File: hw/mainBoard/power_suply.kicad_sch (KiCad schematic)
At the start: 3 parts, among them U2 AMS1117-3.3

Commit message: hw
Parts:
- removed C4, C5: 22uF, symbol Device:C
- removed U2: AMS1117-3.3, Package_TO_SOT_SMD:SOT-223-3_TabPin2, symbol Regulator_Linear:AMS1117-3.3
- added C11: 2.2uF, symbol Device:C
- added C12, C14: 100nF, symbol Device:C
- added C13: 4.7uF, symbol Device:C
- added C15: 10uF, symbol Device:C
- added L1: 2.7uH, symbol Device:L
- added Q1, Q2: NMOS, symbol Simulation_SPICE:NMOS
- added R10: 25m, symbol Device:R
- added R4, R5: 100k, symbol Device:R
- added R6: 40.2k, symbol Device:R
- added R7: 9.53k, symbol Device:R
- added R8: 59k, symbol Device:R
- added R9: 10k, symbol Device:R
- added U2: LM5148RGYR, VQFN24_RGY_TEX, symbol LM5148:LM5148RGYR
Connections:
- net GND: now also C11.2, C12.2, C13.2, C15.2, Q2.3 (S), R6.1, R7.1, R9.1, U2.10 (PGND), U2.16 (VCCX), U2.25 (EPAD), U2.7 (AGND)
- new net: R6.2, U2.3 (CNFG)
- new net: C14.1, L1.2, Q1.3 (S), Q2.1 (D), U2.14 (SW)
- new net: C14.2, U2.15 (CBOOT)
- new net: C12.1, R5.2, U2.18 (PFM/SYNC), U2.8 (VDDA)
- new net: C11.1, R4.2, U2.9 (VCC)
- new net: R8.1, R9.2, U2.6 (FB)
- new net: L1.1, R10.2, U2.20 (ISNS+)
- new net: Q1.2 (G), U2.13 (HO)
- new net: Q2.2 (G), U2.11 (LO)
- new net: R4.1, U2.17 (PG/SYNCOUT)
- new net: R7.2, U2.4 (RT)
- new net: R5.1, U2.5 (EXTCOMP)
- new net 5.5V: C15.1, R10.1, R8.2, U2.21 (VOUT)
- new net EXT_24V: C13.1, Q1.1 (D), U2.12 (VIN)
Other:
- note added: "Output from buck"
- note added: "TODO: change to 5.2V"
- note removed: "Need to be changed to at least 12 V and to use different parts..."

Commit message: hw + blok schema
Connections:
- net EXT_24V renamed 24V
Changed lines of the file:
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@@
     (effects (font (size 1.27 1.27)) (justify left bottom))
   )
-  (global_label "5.5V" (shape input) (at 121.92 31.75 180) (fields_autoplaced)
+  (hierarchical_label "24V" (shape input) (at 160.02 68.58 180) (fields_autoplaced)
     (effects (font (size 1.27 1.27)) (justify right))
-    (property "Intersheetrefs" "${INTERSHEET_REFS}" (at 114.8224 31.75 0)
-      (effects (font (size 1.27 1.27)) (justify right) hide)
-    )
   )
-  (global_label "EXT_24V" (shape input) (at 160.02 68.58 180) (fields_autoplaced)
+  (hierarchical_label "5.5V" (shape output) (at 121.92 31.75 180) (fields_autoplaced)
     (effects (font (size 1.27 1.27)) (justify right))
-    (property "Intersheetrefs" "${INTERSHEET_REFS}" (at 149.2335 68.58 0)
-      (effects (font (size 1.27 1.27)) (justify right) hide)
-    )
   )
   (symbol (lib_id "Device:R") (at 34.29 85.09 180) (unit 1)

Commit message: schematka
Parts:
- removed C11: 2.2uF, symbol Device:C
- removed C12, C14: 100nF, symbol Device:C
- removed C13: 4.7uF, symbol Device:C
- removed C15: 10uF, symbol Device:C
- removed L1: 2.7uH, symbol Device:L
- removed Q1, Q2: NMOS, symbol Simulation_SPICE:NMOS
- removed R10: 25m, symbol Device:R
- removed R4, R5: 100k, symbol Device:R
- removed R6: 40.2k, symbol Device:R
- removed R7: 9.53k, symbol Device:R
- removed R8: 59k, symbol Device:R
- removed R9: 10k, symbol Device:R
- removed U2: LM5148RGYR, VQFN24_RGY_TEX, symbol LM5148:LM5148RGYR
- added C10, C17: 100nF, symbol Device:C
- added C16: 2.2uF, symbol Device:C
- added C8: 10uF, symbol Device:C
- added C9: 4.7uF, symbol Device:C
- added L2: 2.7uH, symbol Device:L
- added Q3, Q4: NMOS, symbol Simulation_SPICE:NMOS
- added R14: 40.2k, symbol Device:R
- added R15: 10k, symbol Device:R
- added R16: 54.9k, symbol Device:R
- added R17: 9.53k, symbol Device:R
- added R18, R19: 100k, symbol Device:R
- added R20: 25m, symbol Device:R
- added U6: LM5148RGYR, VQFN24_RGY_TEX, symbol LM5148:LM5148RGYR
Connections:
- net 24V: now also C9.1, Q3.1 (D), U6.12 (VIN), U6.19 (EN)
- net GND: now also C10.2, C16.2, C8.2, C9.2, Q4.3 (S), R14.1, R15.2, R17.2, U6.10 (PGND), U6.16 (VCCX), U6.25 (EPAD), U6.7 (AGND)
- new net: C16.1, R19.1, U6.9 (VCC)
- new net: R17.1, U6.4 (RT)
- new net: C17.2, L2.2, Q3.3 (S), Q4.1 (D), U6.14 (SW)
- new net: C17.1, U6.15 (CBOOT)
- new net: R18.2, U6.5 (EXTCOMP)
- new net: Q4.2 (G), U6.11 (LO)
- new net: Q3.2 (G), U6.13 (HO)
- new net: R19.2, U6.17 (PG/SYNCOUT)
- new net: R14.2, U6.3 (CNFG)
- new net: R15.1, R16.2, U6.6 (FB)
- new net 5.2V: C8.1, R16.1, R20.1, U6.21 (VOUT)
- new net ISNS+: L2.1, R20.2, U6.20 (ISNS+)
- new net VDDA: C10.1, R18.1, U6.18 (PFM/SYNC), U6.8 (VDDA)
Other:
- note added: "From external power suply"
- note removed: "TODO: change to 5.2V"

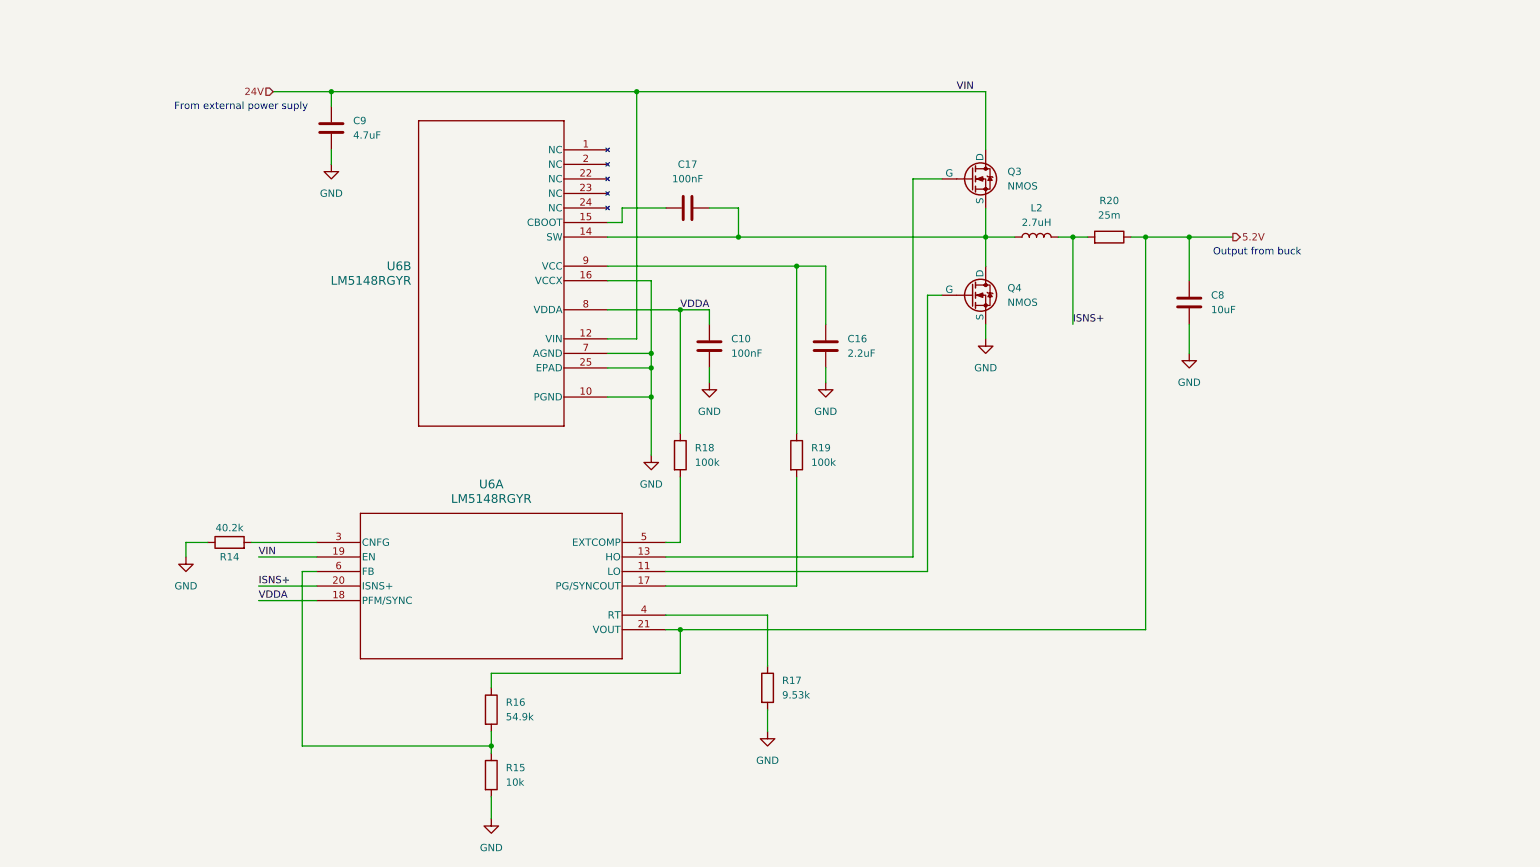
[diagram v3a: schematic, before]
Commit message: text - napajeci obvod, ochrany, 230v + pomocne schema v kicadu
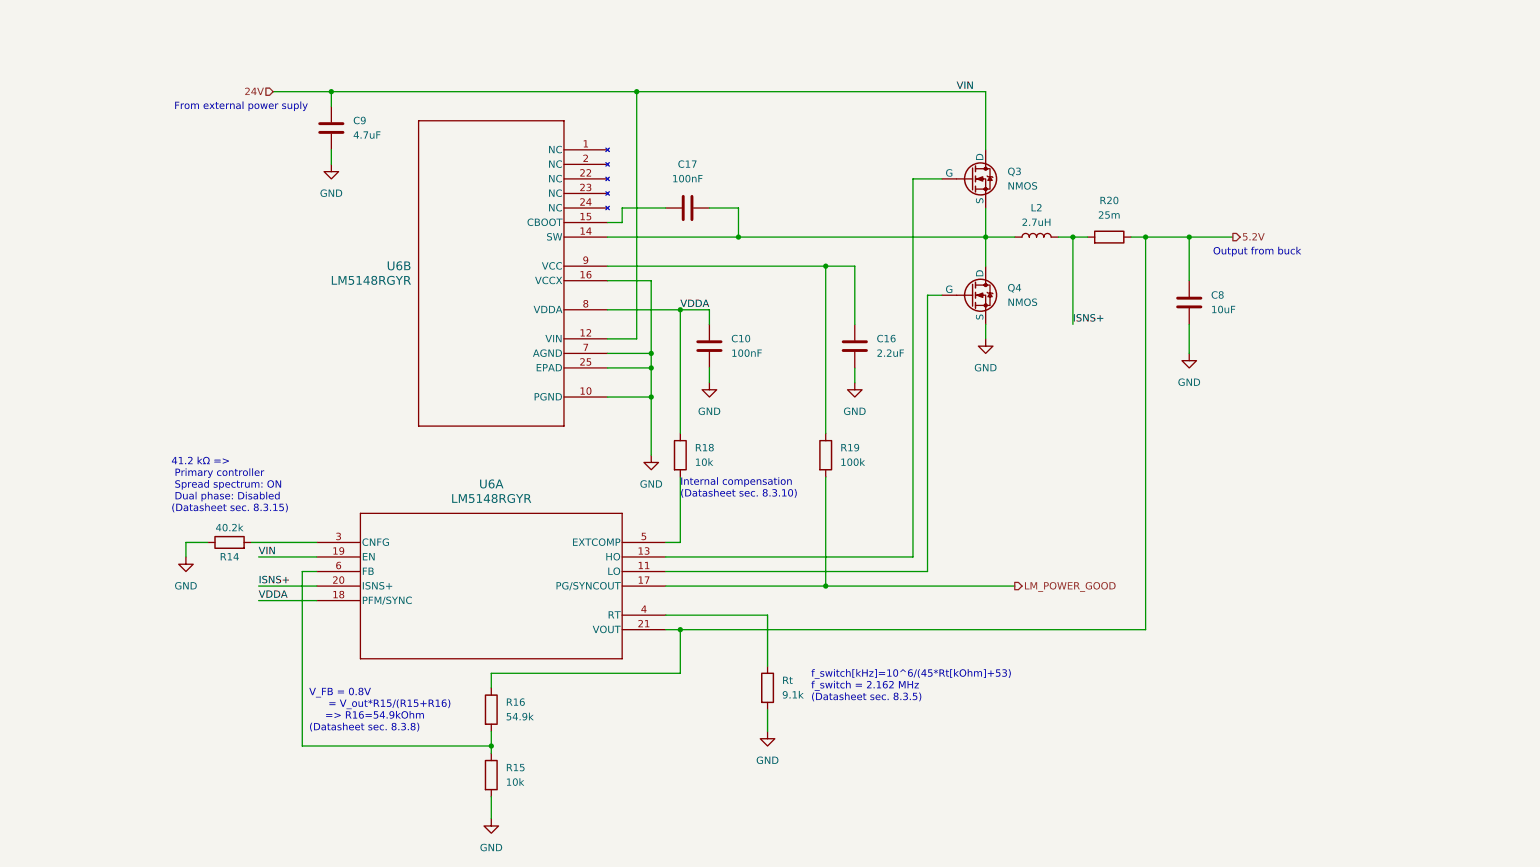
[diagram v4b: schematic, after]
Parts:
- R18: value 100k -> 10k
- Rt: renamed from R17; value 9.53k -> 9.1k
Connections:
- net LM_POWER_GOOD: now reaches R19.2, U6.17 (PG/SYNCOUT)
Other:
- note added: "41.2 kΩ => Primary controller Spread spectrum: ON Dual phase: Disabled (Datasheet sec. 8.3.15)"
- note added: "Internal compensation (Datasheet sec. 8.3.10)"
- note added: "V_FB = 0.8V = V_out*R15/(R15+R16) => R16=54.9kOhm (Datasheet sec. 8.3.8)"
- note added: "f_switch[kHz]=10^6/(45*Rt[kOhm]+53) f_switch = 2.162 MHz (Datasheet sec. 8.3.5)"
- moved on the sheet: C16, R19
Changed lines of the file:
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@@
   (junction (at 76.2 30.48) (diameter 0) (color 0 0 0 0)
   )
+  (junction (at 162.56 60.96) (diameter 0) (color 0 0 0 0)
+  )
   (junction (at 104.14 144.78) (diameter 0) (color 0 0 0 0)
   )
   (junction (at 147.32 55.88) (diameter 0) (color 0 0 0 0)
   )
+  (junction (at 162.56 116.84) (diameter 0) (color 0 0 0 0)
+  )
   (junction (at 132.08 78.74) (diameter 0) (color 0 0 0 0)
   )
@@
   (junction (at 137.16 124.46) (diameter 0) (color 0 0 0 0)
   )
-  (junction (at 157.48 60.96) (diameter 0) (color 0 0 0 0)
-  )
   (junction (at 132.08 83.82) (diameter 0) (color 0 0 0 0)
   )
@@
     (stroke (width 0) (type default))
   )
-  (wire (pts (xy 162.56 78.74) (xy 162.56 81.28))
+  (wire (pts (xy 167.64 78.74) (xy 167.64 81.28))
     (stroke (width 0) (type default))
   )
@@
     (stroke (width 0) (type default))
   )
+  (wire (pts (xy 162.56 60.96) (xy 167.64 60.96))
+    (stroke (width 0) (type default))
+  )
   (wire (pts (xy 129.54 30.48) (xy 129.54 73.66))
     (stroke (width 0) (type default))
@@
     (stroke (width 0) (type default))
   )
-  (wire (pts (xy 157.48 60.96) (xy 162.56 60.96))
-    (stroke (width 0) (type default))
-  )
   (wire (pts (xy 134.62 124.46) (xy 137.16 124.46))
     (stroke (width 0) (type default))
@@
     (stroke (width 0) (type default))
   )
-  (wire (pts (xy 157.48 60.96) (xy 124.46 60.96))
+  (wire (pts (xy 162.56 116.84) (xy 195.58 116.84))
     (stroke (width 0) (type default))
   )
@@
     (stroke (width 0) (type default))
   )
+  (wire (pts (xy 124.46 60.96) (xy 162.56 60.96))
+    (stroke (width 0) (type default))
+  )
   (wire (pts (xy 205.74 71.12) (xy 205.74 55.88))
     (stroke (width 0) (type default))
@@
     (stroke (width 0) (type default))
   )
-  (wire (pts (xy 157.48 97.79) (xy 157.48 116.84))
+  (wire (pts (xy 162.56 97.79) (xy 162.56 116.84))
     (stroke (width 0) (type default))
   )
@@
     (stroke (width 0) (type default))
   )
-  (wire (pts (xy 134.62 116.84) (xy 157.48 116.84))
+  (wire (pts (xy 134.62 116.84) (xy 162.56 116.84))
     (stroke (width 0) (type default))
   )
@@
     (stroke (width 0) (type default))
   )
-  (wire (pts (xy 157.48 90.17) (xy 157.48 60.96))
+  (wire (pts (xy 162.56 90.17) (xy 162.56 60.96))
     (stroke (width 0) (type default))
   )
@@
     (stroke (width 0) (type default))
   )
-  (wire (pts (xy 162.56 71.12) (xy 162.56 60.96))
+  (wire (pts (xy 167.64 71.12) (xy 167.64 60.96))
     (stroke (width 0) (type default))
   )
@@
   )
   (text "From external power suply" (at 48.7471 33.9083 0)
+    (effects (font (size 1.27 1.27)) (justify left bottom))
+  )
+  (text "f_switch[kHz]=10^6/(45*Rt[kOhm]+53)\nf_switch = 2.162 MHz\n(Datasheet sec. 8.3.5)"
+    (at 160.02 137.16 0)
     (effects (font (size 1.27 1.27)) (justify left bottom))
   )
@@
     (effects (font (size 1.27 1.27)) (justify right bottom))
   )
+  (text "41.2 kΩ =>\n Primary controller\n Spread spectrum: ON\n Dual phase: Disabled\n(Datasheet sec. 8.3.15)"
+    (at 48.26 104.14 0)
+    (effects (font (size 1.27 1.27)) (justify left bottom))
+  )
+  (text "Internal compensation\n(Datasheet sec. 8.3.10)" (at 137.16 101.6 0)
+    (effects (font (size 1.27 1.27)) (justify left bottom))
+  )
+  (text "V_FB = 0.8V \n      = V_out*R15/(R15+R16)\n	 => R16=54.9kOhm\n(Datasheet sec. 8.3.8)"
+    (at 72.3291 142.4326 0)
+    (effects (font (size 1.27 1.27)) (justify left bottom))
+  )
   (label "ISNS+" (at 205.74 71.12 0) (fields_autoplaced)
     (effects (font (size 1.27 1.27)) (justify left bottom))
@@
   (label "VDDA" (at 63.5 119.38 0) (fields_autoplaced)
     (effects (font (size 1.27 1.27)) (justify left bottom))
+  )
+  (hierarchical_label "LM_POWER_GOOD" (shape output) (at 195.58 116.84 0) (fields_autoplaced)
+    (effects (font (size 1.27 1.27)) (justify left))
   )
   (hierarchical_label "24V" (shape input) (at 66.04 30.48 180) (fields_autoplaced)
@@
     )
   )
-  (symbol (lib_id "Device:C") (at 162.56 74.93 0) (unit 1)
-    (in_bom yes) (on_board yes) (dnp no) (fields_autoplaced)
-    (property "Reference" "C16" (at 166.37 73.66 0)
-      (effects (font (size 1.27 1.27)) (justify left))
-    )
-    (property "Value" "2.2uF" (at 166.37 76.2 0)
-      (effects (font (size 1.27 1.27)) (justify left))
-    )
-    (property "Footprint" "" (at 163.5252 78.74 0)
-      (effects (font (size 1.27 1.27)) hide)
-    )
-    (property "Datasheet" "~" (at 162.56 74.93 0)
+  (symbol (lib_id "Device:C") (at 167.64 74.93 0) (unit 1)
+    (in_bom yes) (on_board yes) (dnp no) (fields_autoplaced)
+    (property "Reference" "C16" (at 171.45 73.66 0)
+      (effects (font (size 1.27 1.27)) (justify left))
+    )
+    (property "Value" "2.2uF" (at 171.45 76.2 0)
+      (effects (font (size 1.27 1.27)) (justify left))
+    )
+    (property "Footprint" "" (at 168.6052 78.74 0)
+      (effects (font (size 1.27 1.27)) hide)
+    )
+    (property "Datasheet" "~" (at 167.64 74.93 0)
       (effects (font (size 1.27 1.27)) hide)
     )
@@
   (symbol (lib_id "Device:R") (at 152.4 134.62 0) (unit 1)
     (in_bom yes) (on_board yes) (dnp no) (fields_autoplaced)
-    (property "Reference" "R17" (at 154.94 133.35 0)
-      (effects (font (size 1.27 1.27)) (justify left))
-    )
-    (property "Value" "9.53k" (at 154.94 135.89 0)
+    (property "Reference" "Rt" (at 154.94 133.35 0)
+      (effects (font (size 1.27 1.27)) (justify left))
+    )
+    (property "Value" "9.1k" (at 154.94 135.89 0)
       (effects (font (size 1.27 1.27)) (justify left))
     )
@@
       (project "mainBoard"
         (path "/afbe4b5f-4e5c-4a12-a44b-208d158a3f7a/d2d24d60-9ae9-4639-8ba0-76ed40df3c00"
-          (reference "R17") (unit 1)
+          (reference "Rt") (unit 1)
         )
       )
@@
       (effects (font (size 1.27 1.27)) (justify left))
     )
-    (property "Value" "100k" (at 139.7 95.25 0)
+    (property "Value" "10k" (at 139.7 95.25 0)
       (effects (font (size 1.27 1.27)) (justify left))
     )
@@
     )
   )
-  (symbol (lib_id "Device:R") (at 157.48 93.98 0) (unit 1)
-    (in_bom yes) (on_board yes) (dnp no) (fields_autoplaced)
-    (property "Reference" "R19" (at 160.02 92.71 0)
-      (effects (font (size 1.27 1.27)) (justify left))
-    )
-    (property "Value" "100k" (at 160.02 95.25 0)
-      (effects (font (size 1.27 1.27)) (justify left))
-    )
-    (property "Footprint" "" (at 155.702 93.98 90)
-      (effects (font (size 1.27 1.27)) hide)
-    )
-    (property "Datasheet" "~" (at 157.48 93.98 0)
+  (symbol (lib_id "Device:R") (at 162.56 93.98 0) (unit 1)
+    (in_bom yes) (on_board yes) (dnp no) (fields_autoplaced)
+    (property "Reference" "R19" (at 165.1 92.71 0)
+      (effects (font (size 1.27 1.27)) (justify left))
+    )
+    (property "Value" "100k" (at 165.1 95.25 0)
+      (effects (font (size 1.27 1.27)) (justify left))
+    )
+    (property "Footprint" "" (at 160.782 93.98 90)
+      (effects (font (size 1.27 1.27)) hide)
+    )
+    (property "Datasheet" "~" (at 162.56 93.98 0)
       (effects (font (size 1.27 1.27)) hide)
     )
@@
     )
   )
-  (symbol (lib_id "power:GND") (at 162.56 81.28 0) (mirror y) (unit 1)
-    (in_bom yes) (on_board yes) (dnp no) (fields_autoplaced)
-    (property "Reference" "#PWR037" (at 162.56 87.63 0)
-      (effects (font (size 1.27 1.27)) hide)
-    )
-    (property "Value" "GND" (at 162.56 86.36 0)
-      (effects (font (size 1.27 1.27)))
-    )
-    (property "Footprint" "" (at 162.56 81.28 0)
-      (effects (font (size 1.27 1.27)) hide)
-    )
-    (property "Datasheet" "" (at 162.56 81.28 0)
-      (effects (font (size 1.27 1.27)) hide)
-    )
+  (symbol (lib_id "power:GND") (at 167.64 81.28 0) (mirror y) (unit 1)
+    (in_bom yes) (on_board yes) (dnp no) (fields_autoplaced)
+    (property "Reference" "#PWR037" (at 167.64 87.63 0)
+      (effects (font (size 1.27 1.27)) hide)
+    )
+    (property "Value" "GND" (at 167.64 86.36 0)
+      (effects (font (size 1.27 1.27)))
+    )
+    (property "Footprint" "" (at 167.64 81.28 0)
+      (effects (font (size 1.27 1.27)) hide)
+    )
+    (property "Datasheet" "" (at 167.64 81.28 0)
+      (effects (font (size 1.27 1.27)) hide)
+    )

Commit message: drawing layout
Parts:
- C10, C16, C17, C8, C9: footprint (none) -> Capacitor_SMD:C_1206_3216Metric_Pad1.33x1.80mm_HandSolder
- L2: footprint (none) -> Inductor_SMD:L_Bourns-SRN8040_8x8.15mm
- Q3: footprint (none) -> DQJ8; symbol Simulation_SPICE:NMOS -> NMOS-CSD18534:CSD18534Q5A
- Q4: footprint (none) -> DQJ0008A; symbol Simulation_SPICE:NMOS -> NMOS-CSD18514:CSD18514Q5A
- R14, R15, R16, R18, R19, R20: footprint (none) -> Resistor_SMD:R_0805_2012Metric_Pad1.20x1.40mm_HandSolder
- Rt1: renamed from Rt; footprint (none) -> Resistor_SMD:R_0805_2012Metric_Pad1.20x1.40mm_HandSolder
- U6: footprint VQFN24_RGY_TEX -> LM5148:VQFN24_RGY_TEX
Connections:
- net 24V: now also Q3.5, Q3.6 (D), Q3.7 (D), Q3.8 (D), Q3.9; no longer Q3.1 (D)
- net GND: now also Q4.1, Q4.2 (S); no longer Q4.3 (S)
- net at C17.2, L2.2, U6.14 (SW): now also Q3.1, Q3.2 (S), Q4.5, Q4.6 (D), Q4.7 (D), Q4.8 (D), Q4.9; no longer Q3.3 (S), Q4.1 (D)
- net at U6.11 (LO): now also Q4.4; no longer Q4.2 (G)
- net at U6.13 (HO): now also Q3.4; no longer Q3.2 (G)
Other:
- moved on the sheet: C9, R14

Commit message: buck vedle
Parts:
- removed Q3: NMOS, DQJ8, symbol NMOS-CSD18534:CSD18534Q5A
- added C15, C18, C19: 47uF, Capacitor_SMD:C_1210_3225Metric_Pad1.33x2.70mm_HandSolder, symbol Device:C
- added C20, C21: 10uF, Capacitor_SMD:C_1210_3225Metric_Pad1.33x2.70mm_HandSolder, symbol Device:C
- added C22: 470nF, Capacitor_SMD:C_0805_2012Metric_Pad1.18x1.45mm_HandSolder, symbol Device:C
- added C23, C24, C25, C26: 0.01uF, Capacitor_SMD:C_0805_2012Metric_Pad1.18x1.45mm_HandSolder, symbol Device:C
- added C27: 22p, Capacitor_SMD:C_0805_2012Metric_Pad1.18x1.45mm_HandSolder, symbol Device:C
- added NT1: NetTie_2, NetTie:NetTie-2_SMD_Pad0.5mm, symbol Device:NetTie_2
- added Q1: NMOS, DQJ0008A, symbol NMOS-CSD18514:CSD18514Q5A
- added R3: 10k, Resistor_SMD:R_0805_2012Metric_Pad1.20x1.40mm_HandSolder, symbol Device:R
- C10, C17: footprint Capacitor_SMD:C_1206_3216Metric_Pad1.33x1.80mm_HandSolder -> Capacitor_SMD:C_0805_2012Metric_Pad1.18x1.45mm_HandSolder
- C16: value 2.2uF -> 4.7uF; footprint Capacitor_SMD:C_1206_3216Metric_Pad1.33x1.80mm_HandSolder -> Capacitor_SMD:C_0805_2012Metric_Pad1.18x1.45mm_HandSolder
- C8: value 10uF -> 47uF; footprint Capacitor_SMD:C_1206_3216Metric_Pad1.33x1.80mm_HandSolder -> Capacitor_SMD:C_1210_3225Metric_Pad1.33x2.70mm_HandSolder
- C9: value 4.7uF -> 2.7nF; footprint Capacitor_SMD:C_1206_3216Metric_Pad1.33x1.80mm_HandSolder -> Capacitor_SMD:C_0805_2012Metric_Pad1.18x1.45mm_HandSolder; now not fitted
- R14: value 40.2k -> 41.2k
- R20: footprint Resistor_SMD:R_0805_2012Metric_Pad1.20x1.40mm_HandSolder -> Resistor_SMD:R_0815_2038Metric_Pad1.20x4.05mm_HandSolder
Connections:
- net 24V: now also C20.1, C21.1, C22.1, C23.1, C24.1, C25.1, C26.1, Q1.5, Q1.6 (D), Q1.7 (D), Q1.8 (D), Q1.9; no longer C9.1
- net 5.2V: now also C15.1, C18.1, C19.1
- net GND: now also C15.2, C18.2, C19.2, C20.2, C21.2, C22.2, C23.2, C24.2, C25.2, C26.2, NT1.2; no longer C10.2, C9.2, R14.1, R15.2, Rt1.2
- net at C17.2, L2.2, Q4.5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: now also Q1.1, Q1.2 (S), Q1.3 (S)
- net at R18.2, U6.5 (EXTCOMP): now also C27.1, R3.1
- net at U6.13 (HO): now also Q1.4
- new net: C9.1, R3.2
- new net GNDA: C10.2, C27.2, C9.2, NT1.1, R14.1, R15.2, Rt1.2
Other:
- note added: "For external compensation"
- moved on the sheet: C10, R18

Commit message: finale bez rybicky
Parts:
- L1: renamed from L2; value 2.7uH -> 3.6uH
- Q1: footprint DQJ0008A -> NMOS-CSD18514:DQJ0008A
- Q2: renamed from Q4; footprint DQJ0008A -> NMOS-CSD18514:DQJ0008A
- R3: renamed from R20; value 25m -> 10m
- Rt1: value 9.1k -> 35.7k
- renumbered C18 to C10, C19 to C11, C24 to C12, C25 to C13, C23 to C14, C21 to C15, C8 to C16, C15 to C17, C26 to C18, C22 to C21, C17 to C22, C10 to C23, C16 to C24, C27 to C25, C20 to C26, C9 to C27, NT1 to NT2, R14 to R4, R3 to R5, R19 to R6, R15 to R7, R16 to R8, R18 to R9, U6 to U4
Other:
- note added: "f_switch[kHz]=10^6/(45*Rt[kOhm]+53) f_switch = 602.59 kHz (Datasheet sec. 8.3.5)"
- note removed: "f_switch[kHz]=10^6/(45*Rt[kOhm]+53) f_switch = 2.162 MHz (Datasheet sec. 8.3.5)"
